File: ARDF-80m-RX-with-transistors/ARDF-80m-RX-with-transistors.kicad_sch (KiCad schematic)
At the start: 45 parts, among them J1 JACK, Q1 BC847, Q2 BC847, Q3 BC847, Q4 BC847, Q5 BC847, U1 LM358, Y1 3.5795MHz

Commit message: Update diodes packaging
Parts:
- D1, D2, D3, D5: footprint Diode_SMD:D_MiniMELF -> Diode_SMD:D_0805_2012Metric_Pad1.15x1.40mm_HandSolder
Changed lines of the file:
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@@
 			)
 		)
-		(property "Footprint" "Diode_SMD:D_MiniMELF"
+		(property "Footprint" "Diode_SMD:D_0805_2012Metric_Pad1.15x1.40mm_HandSolder"
 			(at 109.22 104.14 0)
 			(effects
@@
 			)
 		)
-		(property "Footprint" "Diode_SMD:D_MiniMELF"
+		(property "Footprint" "Diode_SMD:D_0805_2012Metric_Pad1.15x1.40mm_HandSolder"
 			(at 109.22 123.19 0)
 			(effects
@@
 			)
 		)
-		(property "Footprint" "Diode_SMD:D_MiniMELF"
+		(property "Footprint" "Diode_SMD:D_0805_2012Metric_Pad1.15x1.40mm_HandSolder"
 			(at 109.22 115.57 0)
 			(effects
@@
 			)
 		)
-		(property "Footprint" "Diode_SMD:D_MiniMELF"
+		(property "Footprint" "Diode_SMD:D_0805_2012Metric_Pad1.15x1.40mm_HandSolder"
 			(at 109.22 130.81 0)
 			(effects

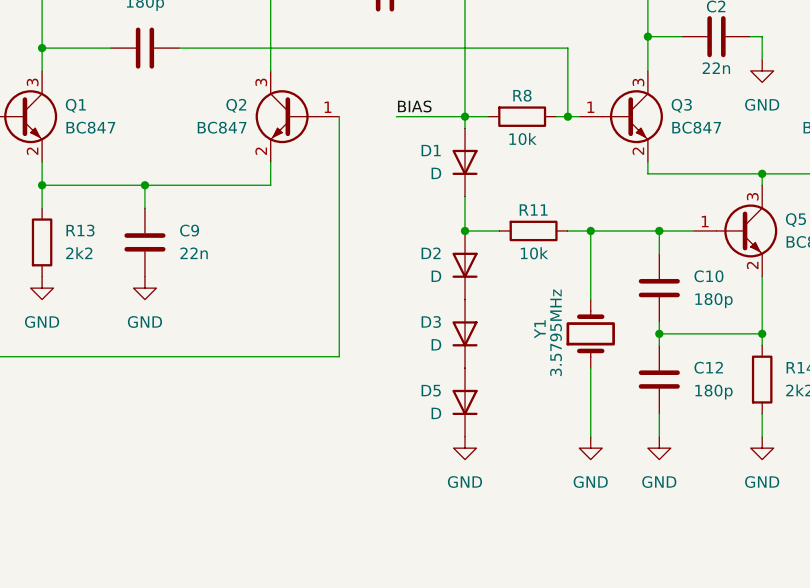
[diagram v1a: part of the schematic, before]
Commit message: Update jack connector footprint
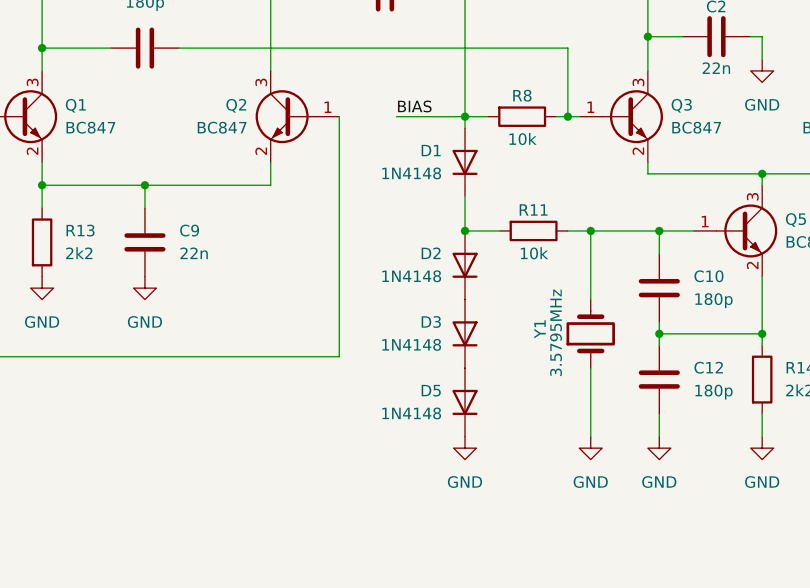
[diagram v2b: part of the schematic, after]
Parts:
- D1, D2, D3, D5: value D -> 1N4148
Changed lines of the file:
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@@
 			)
 		)
-		(property "Value" "D"
+		(property "Value" "1N4148"
 			(at 106.68 105.4099 90)
 			(effects
@@
 			)
 		)
-		(property "Value" "D"
+		(property "Value" "1N4148"
 			(at 106.68 124.4599 90)
 			(effects
@@
 			)
 		)
-		(property "Value" "D"
+		(property "Value" "1N4148"
 			(at 106.68 116.8399 90)
 			(effects
@@
 			)
 		)
-		(property "Value" "D"
+		(property "Value" "1N4148"
 			(at 106.68 132.0799 90)
 			(effects
